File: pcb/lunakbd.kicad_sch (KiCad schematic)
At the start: 72 parts, among them J1 TRRS-PJ-320D, J2 Battery_Socket, J3 Conn_Display, SW1 Switch, SW10 Switch, SW11 Switch, SW12 Switch, SW13 Switch, SW14 Switch, SW15 Switch, SW16 Switch, SW17 Switch, SW18 Switch, SW19 Switch, SW2 Switch, SW20 Switch, SW21 Switch, SW22 Switch, SW23 Switch, SW24 Switch, SW25 Switch, SW26 Switch, SW27 Switch, SW28 Switch, SW29 RotaryEncoder_SW, SW3 Switch, SW30 Reset_Button, SW31 Battery_Switch, SW4 Switch, SW5 Switch, SW6 Switch, SW7 Switch, SW8 Switch, SW9 Switch, U1 ProMicro

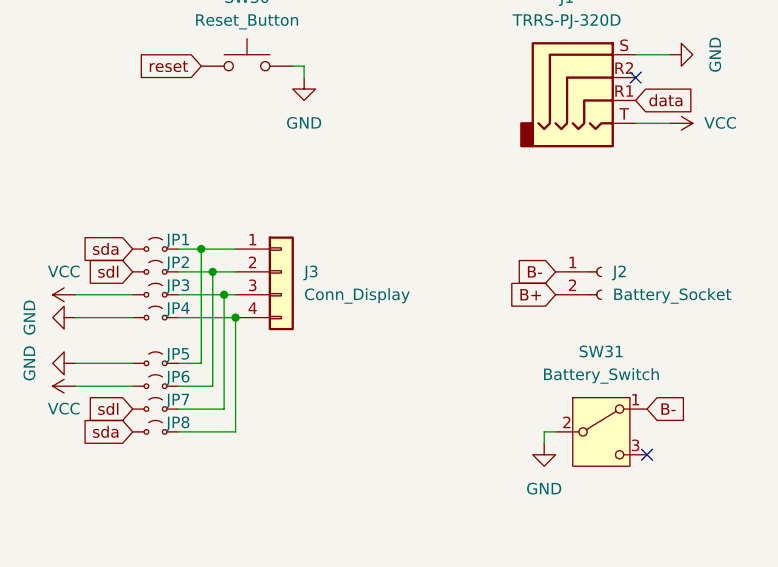
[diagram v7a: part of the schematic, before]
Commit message: refactor: update all footprints and fix thumb keys align
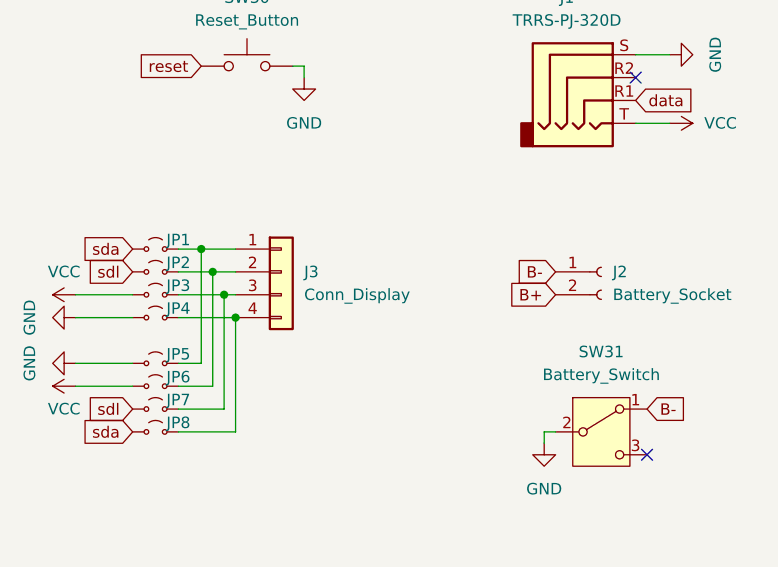
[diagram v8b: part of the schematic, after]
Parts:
- D1, D10, D11, D12, D13, D14, D15, D16, D17, D18, D19, D2, D20, D21, D22, D23, D24, D25, D26, D27, D28, D29, D3, D4, D5, D6, D7, D8, D9: footprint Library:D_SOD-123 -> lunalib:D_SOD-123
- J1: footprint Library:TRRS-PJ-320D -> lunalib:TRRS-PJ-320D
- J2: footprint Connector_JST:JST_PH_S2B-PH-K_1x02_P2.00mm_Horizontal -> lunalib:JST_PH_S2B-PH-K_1x02_P2.00mm_Horizontal
- J3: footprint kbd:OLED -> lunalib:OLED
- JP1, JP2, JP3, JP4, JP5, JP6, JP7, JP8: footprint Jumper:SolderJumper-2_P1.3mm_Open_RoundedPad1.0x1.5mm -> lunalib:SolderJumper-2_P1.3mm_Open_RoundedPad1.0x1.5mm
- SW1, SW10, SW11, SW12, SW13, SW14, SW15, SW16, SW17, SW18, SW19, SW2, SW20, SW21, SW22, SW23, SW24, SW25, SW26, SW27, SW3, SW4, SW5, SW6, SW7, SW8, SW9: footprint Library:SW_Hotswap_Kailh_MX_1.00u -> lunalib:SW_Hotswap_Kailh_MX_1.00u
- SW28: footprint Library:SW_Hotswap_Kailh_MX_1.25u_90deg -> lunalib:SW_Hotswap_Kailh_MX_1.25u_90deg
- SW29: footprint Rotary_Encoder:RotaryEncoder_Alps_EC11E-Switch_Vertical_H20mm -> lunalib:RotaryEncoder_Alps_EC11E-Switch_Vertical_H20mm
- SW30: footprint Library:SW_TL3330AF130QG -> lunalib:SW_TL3330AF130QG
- SW31: footprint Library:SW_MSK12C02-HB -> lunalib:SW_MSK12C02-HB
- U1: footprint PCM_marbastlib-xp-promicroish:SuperMini_nRF52840_H_USBup -> lunalib:SuperMini_nRF52840
